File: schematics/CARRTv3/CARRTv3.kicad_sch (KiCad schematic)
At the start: 26 parts, among them J1 LCD_with_5_Buttons, M1 Rear Right, M2 Front Right, M3 Front Left, M4 Rear Left, P1 PowerBoost_1000C, SW1 On-Off Master Switch, SW2 RPi0 Shutdown, SW3 Right Encoder, SW4 Left Encoder, T1 2N2222, U1 BNO055, X1 Raspberry_Pi_Zero2, X2 Raspberry_Pico2

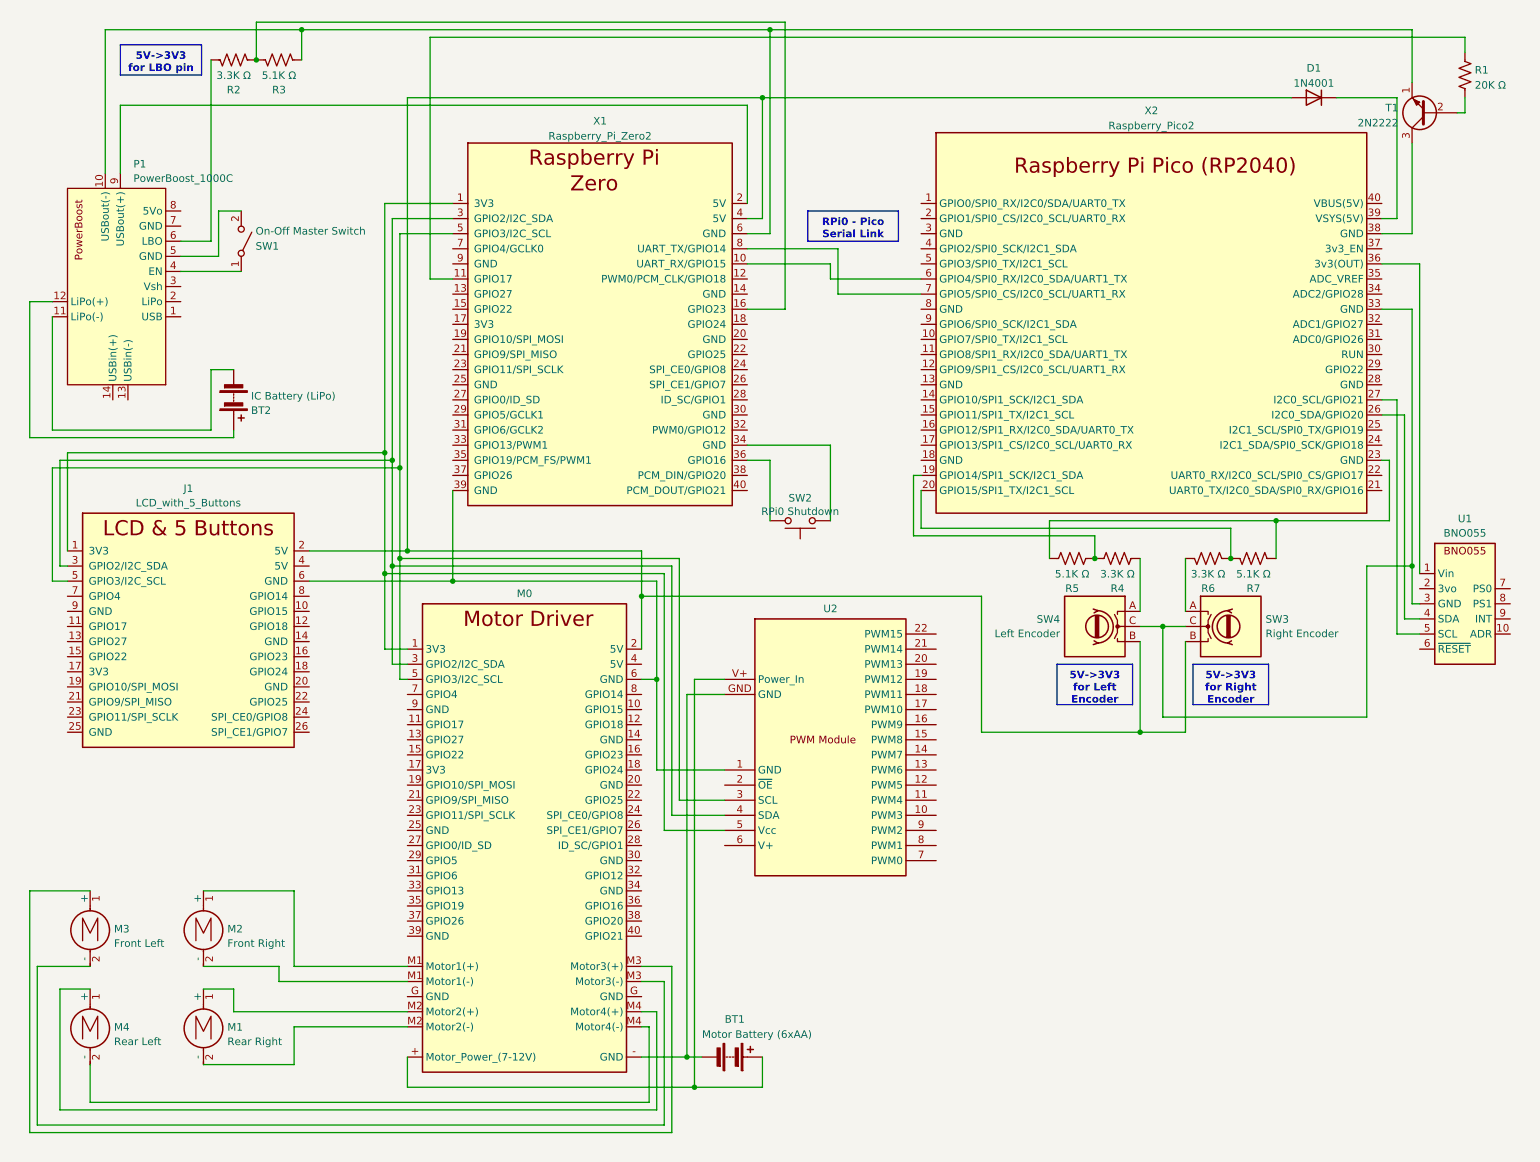
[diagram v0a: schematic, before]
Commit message: Added level-shifters, LIDAR, etc
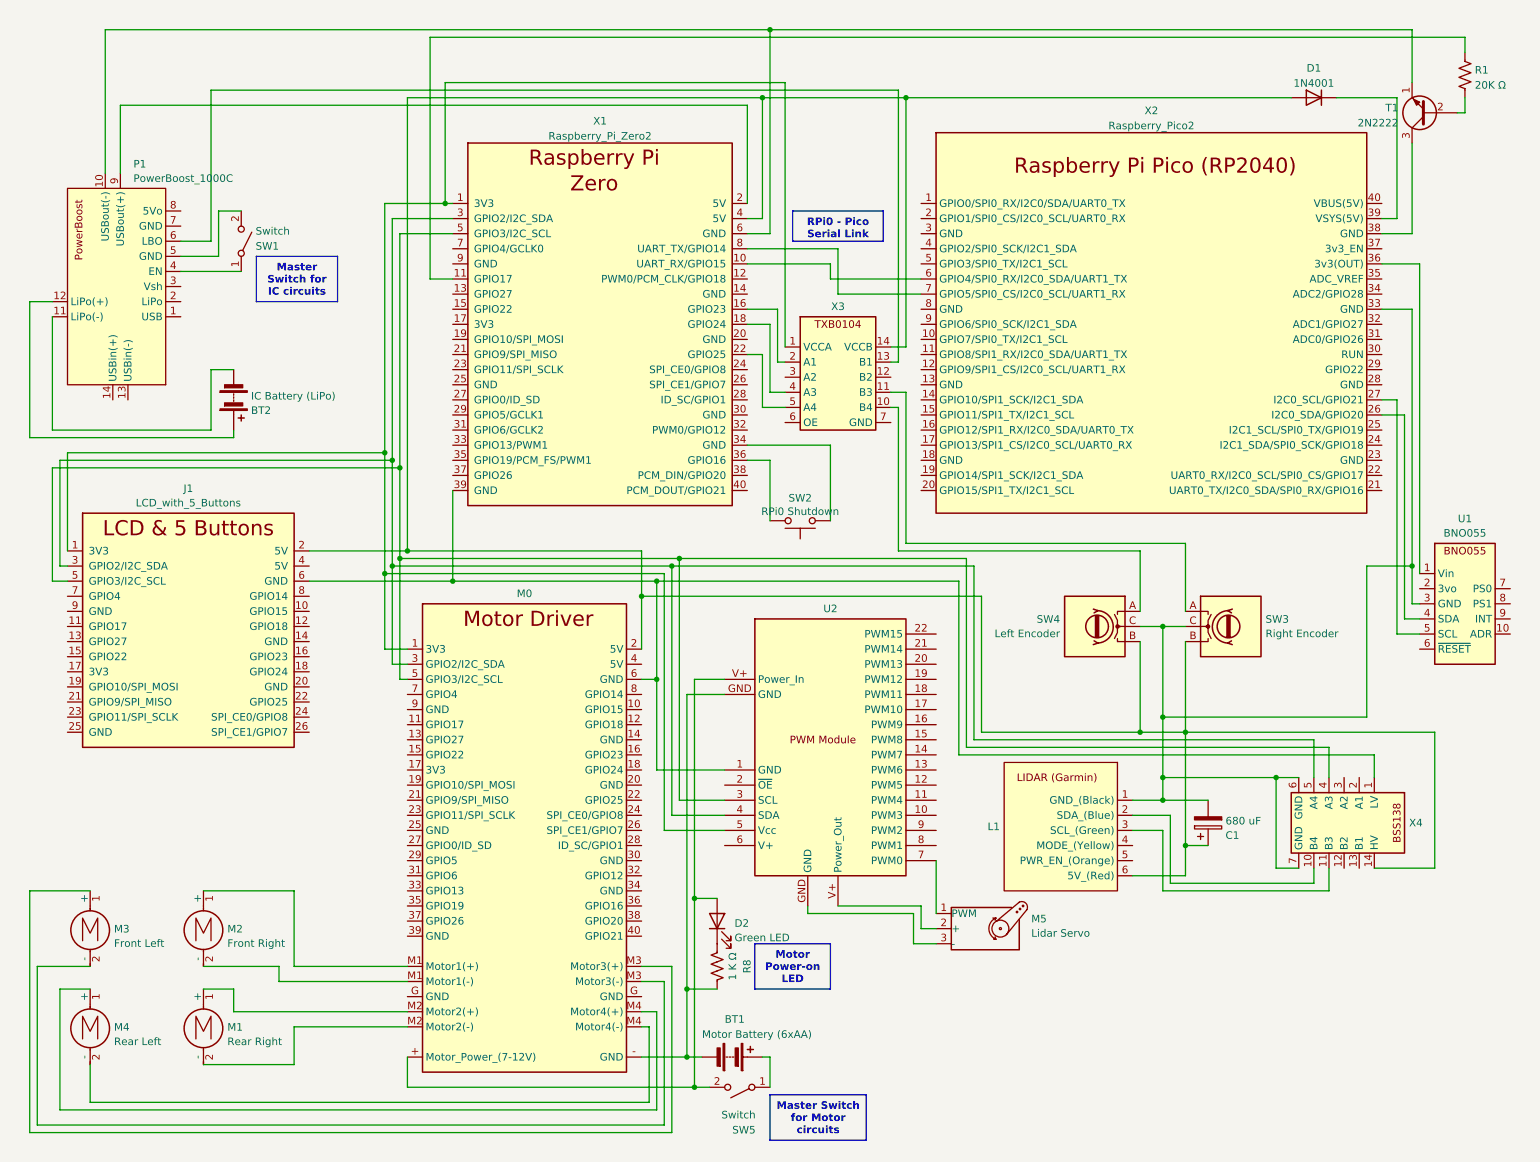
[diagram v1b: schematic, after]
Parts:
- removed R2, R4, R6: 3.3K Ω, symbol Device:R_US
- removed R3, R5, R7: 5.1K Ω, symbol Device:R_US
- added C1: 680 uF, symbol Device:C_Polarized
- added D2: Green LED, symbol Device:LED
- added L1: ~, symbol CARRTv3:LIDAR
- added M5: Lidar Servo, symbol Motor:Motor_Servo
- added R8: 1 K Ω, symbol Device:R_US
- added SW5: Switch, symbol Switch:SW_SPST
- added X3: ~, symbol CARRTv3:TXB0104
- added X4: ~, symbol CARRTv3:BSS138
- SW1: value On-Off Master Switch -> Switch
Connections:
- net at BT1.2 (-), M0.- (GND), U2.GND: now also R8.2
- net at SW4.A: now also X3.10 (B4)
- net at D1.2 (A), J1.2 (5V), M0.2 (5V)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: now also C1.1, L1.6 (5V_(Red)), X3.14 (VCCB), X4.14 (HV)
- net at SW3.C, SW4.C, U1.3 (GND)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: now also C1.2, L1.1 (GND_(Black)), X4.6 (GND), X4.7 (GND)
- net at P1.6 (LBO): now also X3.13 (B1)
- net at SW3.A: now also X3.11 (B3)
- net at J1.1 (3V3), M0.1 (3V3), U2.5 (Vcc)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: now also X3.1 (VCCA)
- net at X1.16 (GPIO23): now also X3.2 (A1)
- net at X1.18 (GPIO24): now also X3.4 (A3)
- net at X1.22 (GPIO25): now also X3.5 (A4)
- net at J1.3 (GPIO2/I2C_SDA), M0.3 (GPIO2/I2C_SDA), U2.4 (SDA)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: now also X4.5 (A4)
- net at J1.6 (GND), M0.6 (GND), U2.1 (GND)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: now also X4.1 (LV)
- net at J1.5 (GPIO3/I2C_SCL), M0.5 (GPIO3/I2C_SCL), U2.3 (SCL)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: now also X4.4 (A3)
- net at U2.7 (PWM0): now also M5.1 (PWM)
- new net: L1.2 (SDA_(Blue)), X4.10 (B4)
- new net: L1.3 (SCL_(Green)), X4.11 (B3)
- new net: BT1.1 (+), SW5.1 (A)
- new net: D2.1 (K), R8.1
- new net: D2.2 (A), M0.+ (Motor_Power_(7-12V)), SW5.2 (B), U2.V+ (Power_Out)
- new net: M5.3 (-), U2.GND
- new net: M5.2 (+), U2.V+ (Power_Out)

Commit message: Updated to use voltage shifters
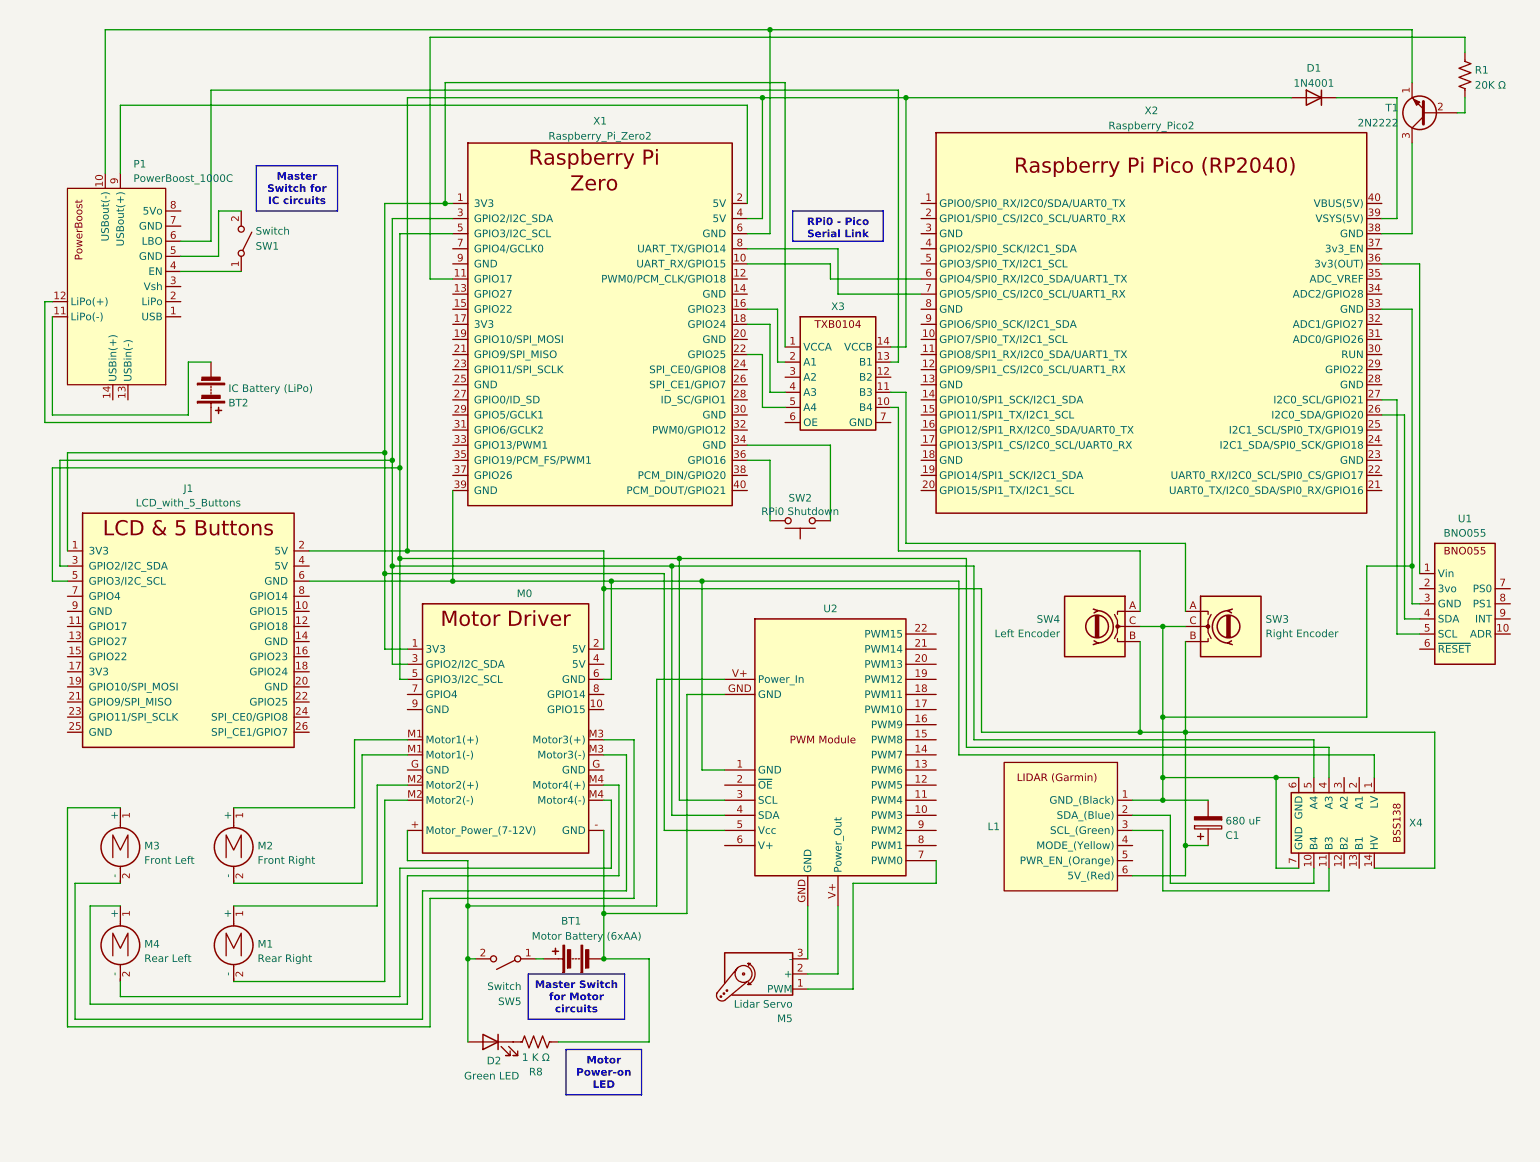
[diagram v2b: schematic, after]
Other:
- moved on the sheet: BT1, BT2, D2, M1, M2, M3, M4, M5, R8, SW5

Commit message: Color-coded the wiring
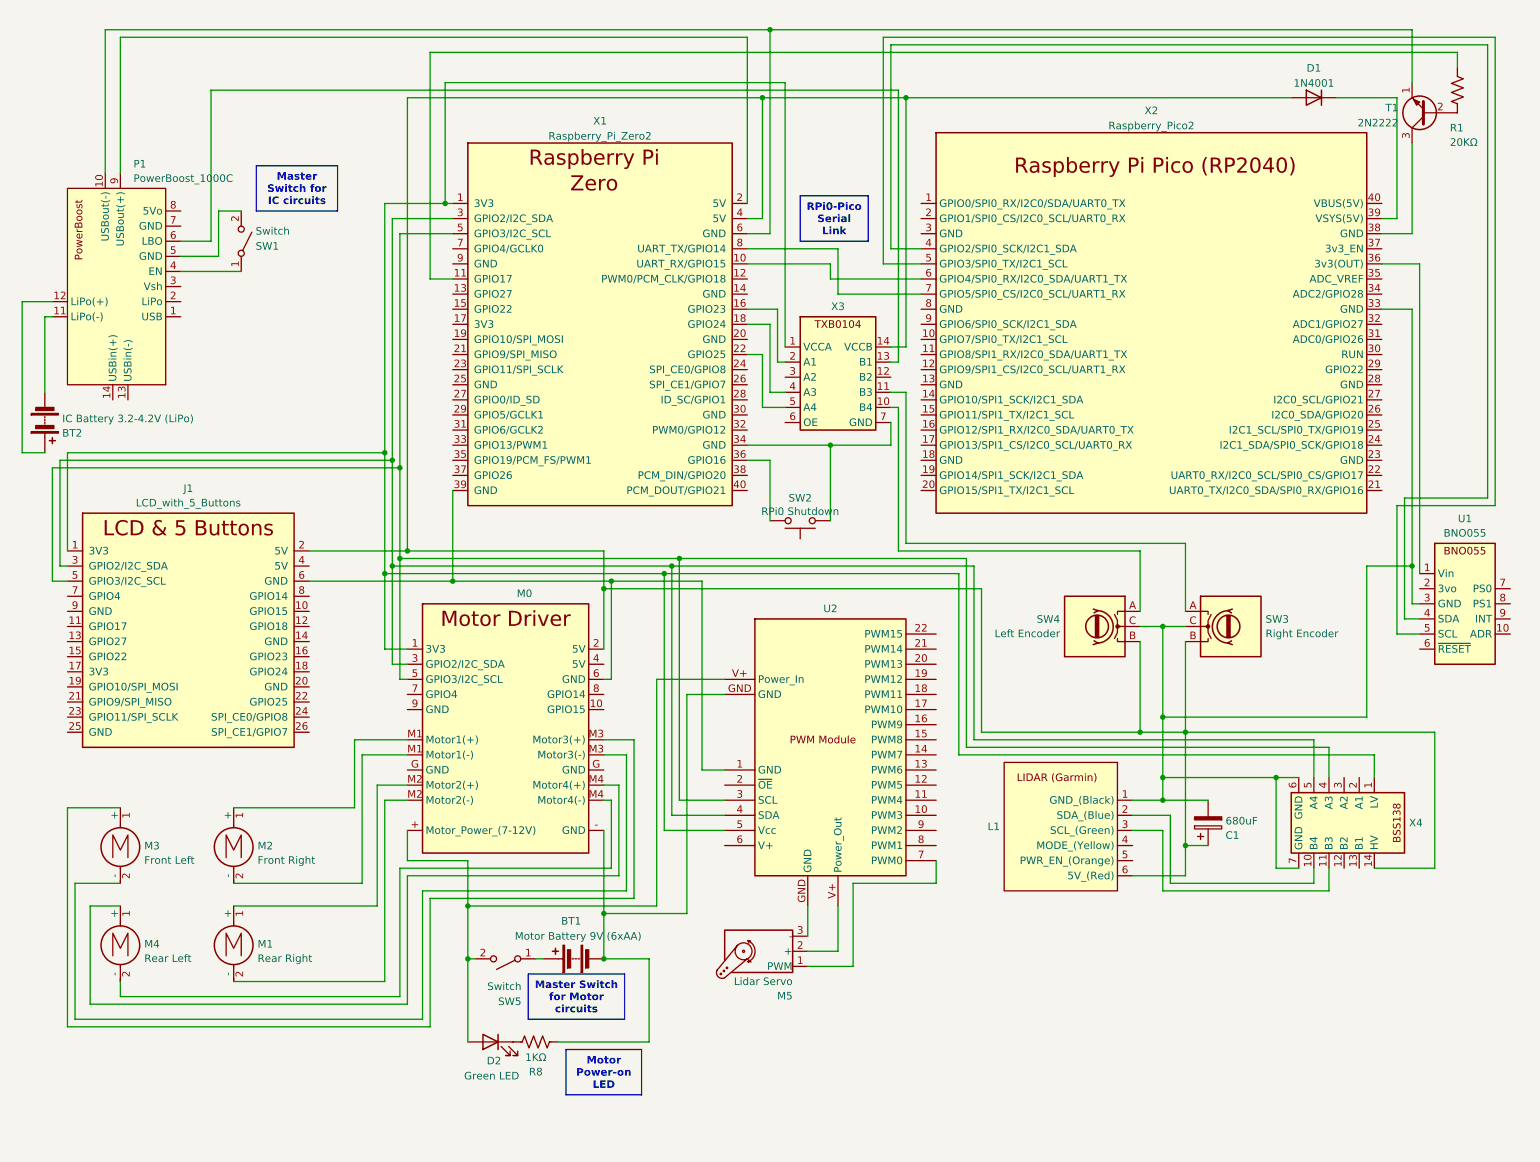
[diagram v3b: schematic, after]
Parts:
- BT1: value Motor Battery (6xAA) -> Motor Battery 9V (6xAA)
- BT2: value IC Battery (LiPo) -> IC Battery 3.2-4.2V (LiPo)
- C1: value 680 uF -> 680uF
- R1: value 20K Ω -> 20KΩ
- R8: value 1 K Ω -> 1KΩ
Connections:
- net at J1.6 (GND), M0.6 (GND), U2.1 (GND)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: no longer X4.1 (LV)
- net at SW2.1, X1.34 (GND): now also X3.7 (GND)
- net at J1.1 (3V3), M0.1 (3V3), U2.5 (Vcc)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: now also X4.1 (LV)
- net at X2.26 (I2C0_SDA/GPIO20): no longer U1.4 (SDA)
- net at X2.27 (I2C0_SCL/GPIO21): no longer U1.5 (SCL)
- net at X2.4 (GPIO2/SPI0_SCK/I2C1_SDA): now also U1.4 (SDA)
- net at X2.5 (GPIO3/SPI0_TX/I2C1_SCL): now also U1.5 (SCL)
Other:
- moved on the sheet: BT2, M5, R1

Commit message: Cleaned up wiring, added labels
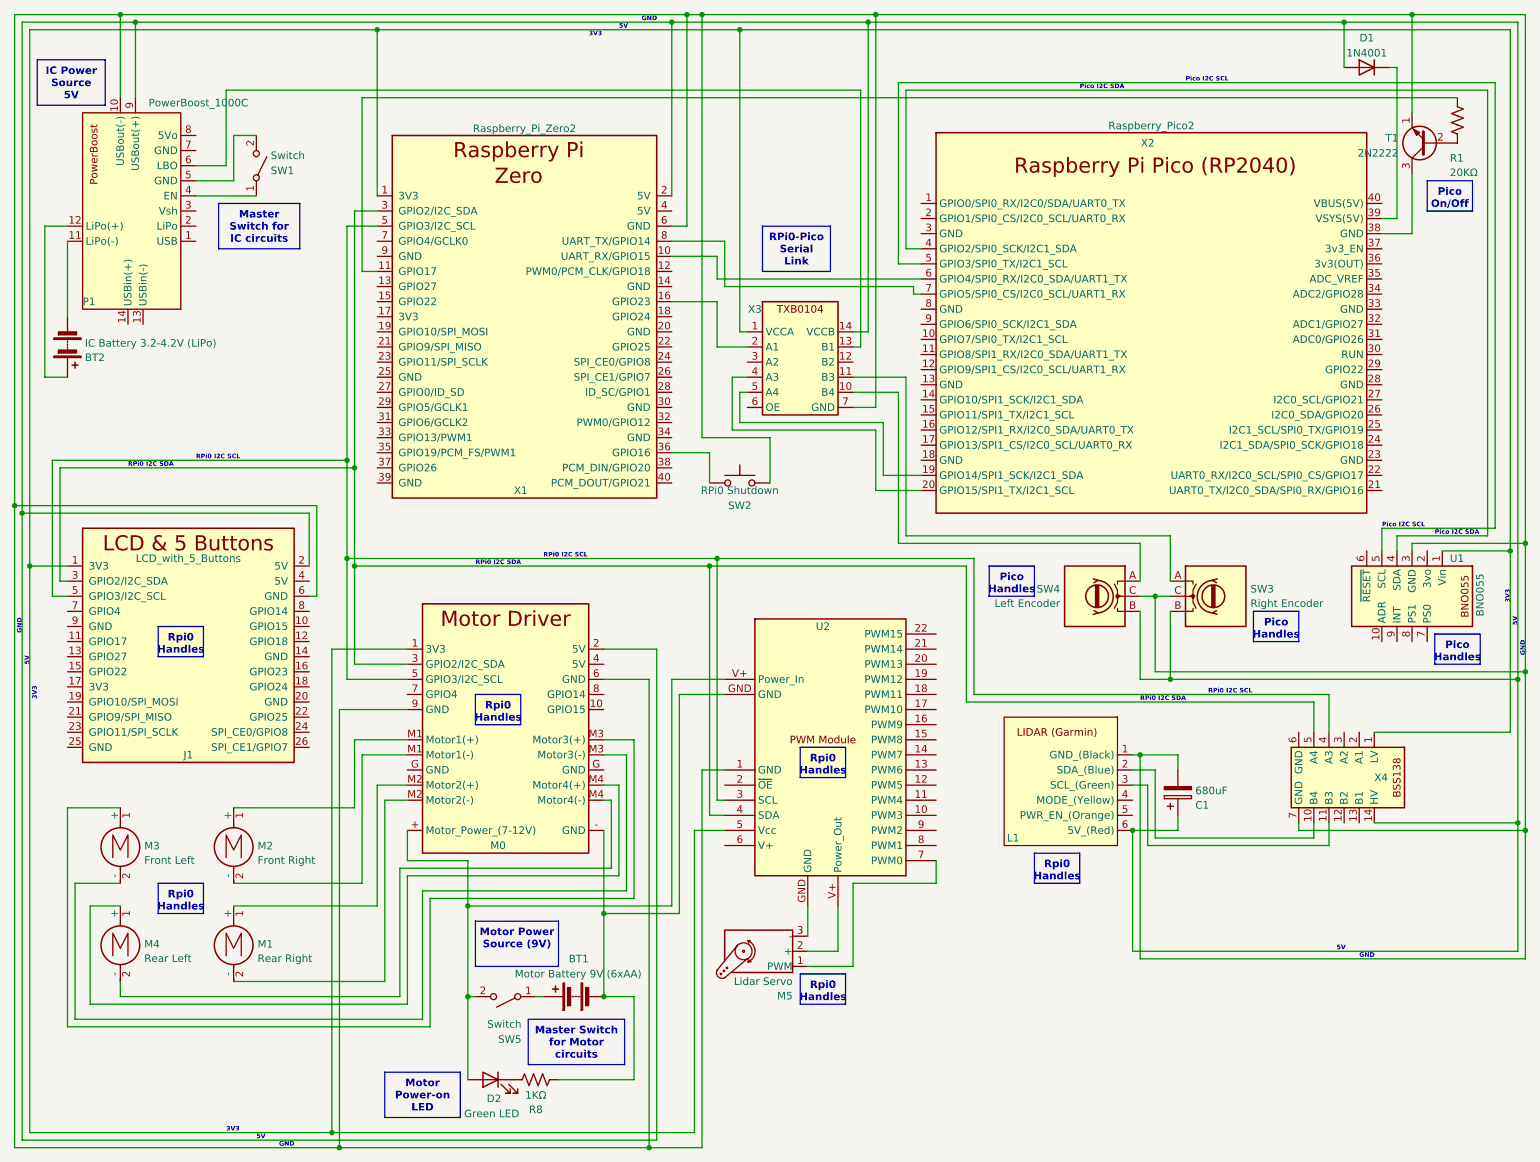
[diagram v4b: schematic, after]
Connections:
- net at J1.1 (3V3), M0.1 (3V3), U2.5 (Vcc)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: now also U1.1 (Vin)
- net at C1.1, D1.2 (A), J1.2 (5V)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: now also P1.9 (USBout(+)), X1.2 (5V); no longer X1.4 (5V)
- net at C1.2, L1.1 (GND_(Black)), SW3.C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: now also J1.6 (GND), M0.6 (GND), M0.9 (GND), P1.10 (USBout(-)), SW2.1, T1.1 (E), U2.1 (GND), X1.6 (GND), X3.7 (GND); no longer X2.33 (GND), X4.6 (GND)
- net at X1.18 (GPIO24): no longer X3.4 (A3)
- net at X1.22 (GPIO25): no longer X3.5 (A4)
- net at X2.19 (GPIO14/SPI1_SCK/I2C1_SDA): now also X3.5 (A4)
- net at X2.20 (GPIO15/SPI1_TX/I2C1_SCL): now also X3.4 (A3)
- net at X2.36 (3v3(OUT)): no longer U1.1 (Vin)
- now unconnected: X1.34 (GND), X1.39 (GND)
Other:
- note added: "3V3"
- note added: "5V"
- note added: "GND"
- note added: "Pico I2C SCL"
- note added: "Pico I2C SDA"
- note added: "RPi0 I2C SCL"
- note added: "RPi0 I2C SDA"
- moved on the sheet: BT1, BT2, C1, D1, D2, J1, L1, P1, R1, R8, SW1, SW2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
